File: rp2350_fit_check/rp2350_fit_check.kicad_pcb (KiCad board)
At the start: 6 copper layers, 118.8 x 73.4 mm, 667 parts, among them J1 Conn_01x05, J2 Conn_01x05, J3 Conn_01x05, J4 Conn_01x05, J5 Conn_01x04, SW1 SW_Push, SW2 SW_Push, U1 AP2112K-3.3, U2 RP2040, U3 W25Q16JVUXIQ_TR, Y1 12MHz, Y1 ABM8-272-T3

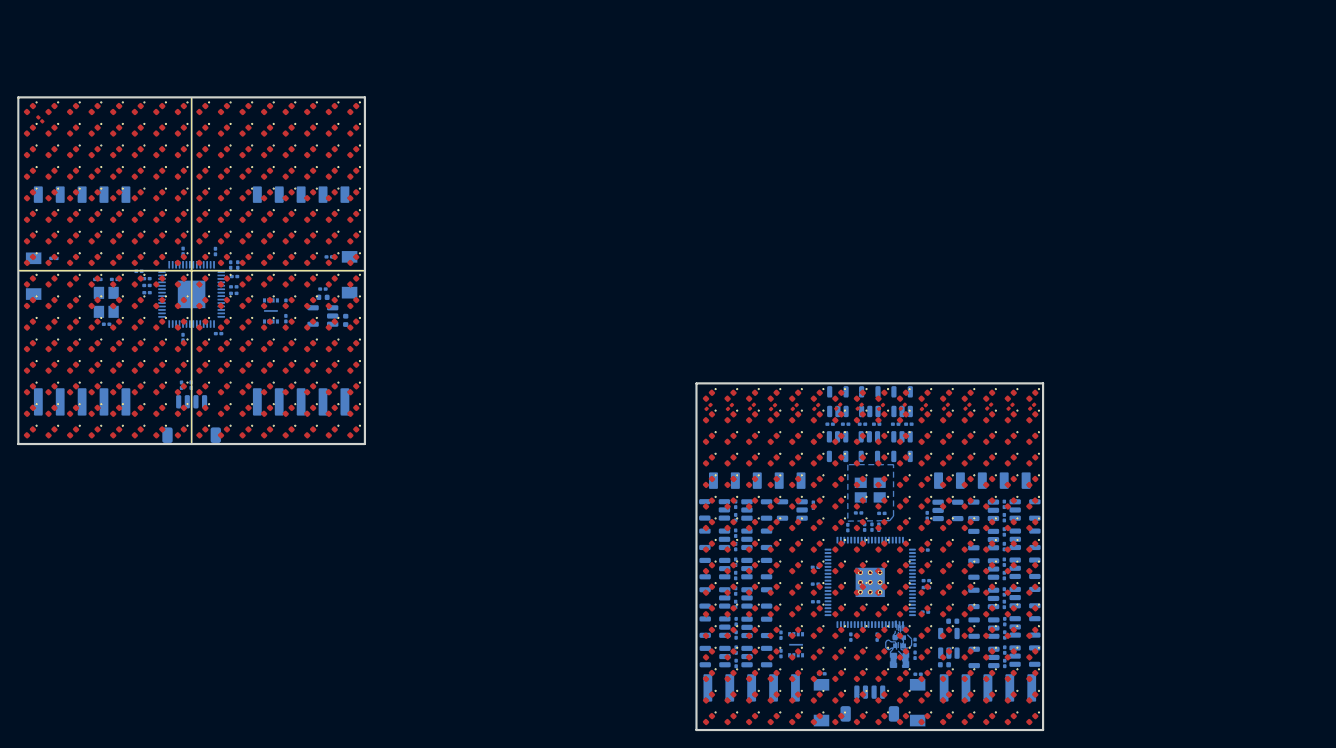
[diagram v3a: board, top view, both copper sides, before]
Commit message: Worked on new 18x18 led version of rp2350 design.
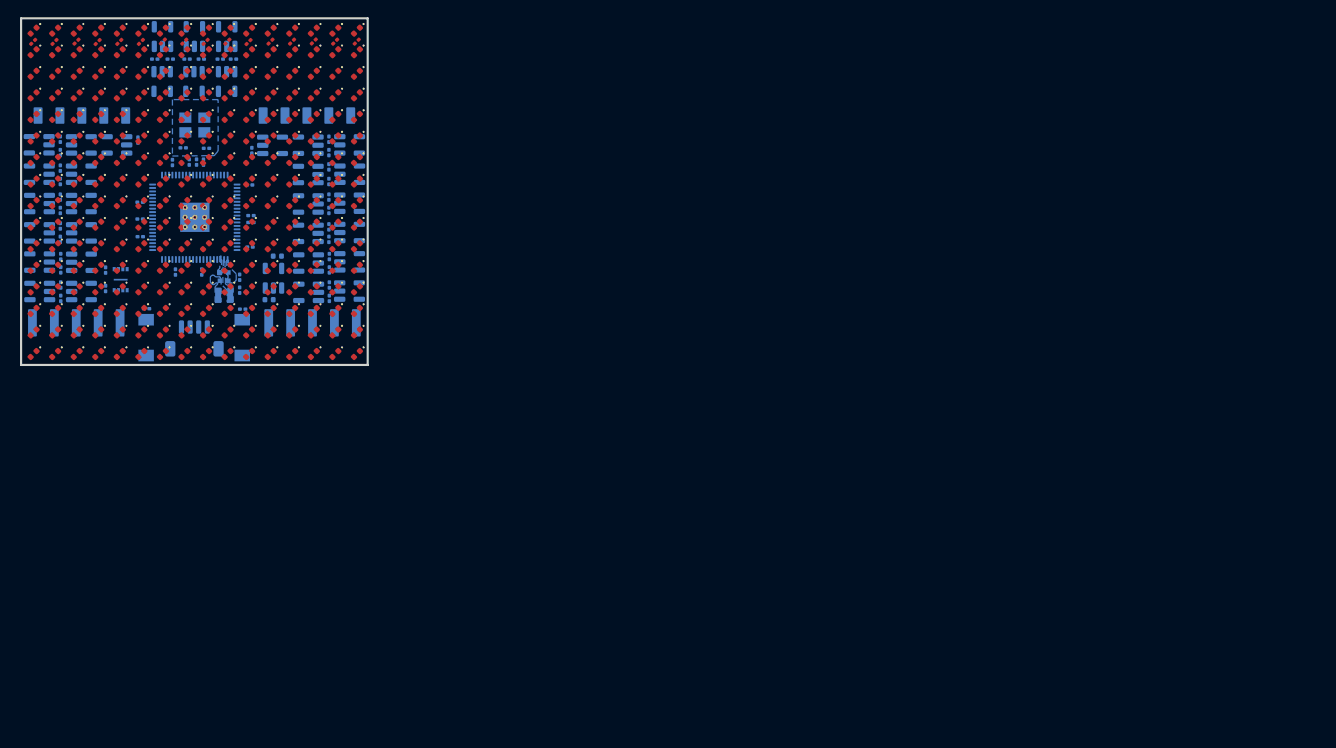
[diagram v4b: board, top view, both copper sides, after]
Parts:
- removed the C1 at (87.9, 75.8)
- removed C10, C9: 1uF, panel_custom:C_0201_0603Metric
- removed C11, C12, C13, C14, C15, C16, C17, C18, C19, C20, C3, C8: 0.1uF, panel_custom:C_0201_0603Metric
- removed the C2 at (85.2, 73.1)
- removed C4, C5: 20pF, panel_custom:C_0201_0603Metric
- removed the C6 at (75.3, 69.3)
- removed the C7 at (75.0, 70.7)
- removed the D1 at (51.2, 51.2)
- removed the D10 at (51.2, 73.8)
- removed the D100 at (66.2, 58.8)
- removed the D101 at (66.2, 61.2)
- removed the D102 at (66.2, 63.8)
- removed the D103 at (66.2, 66.2)
- removed the D104 at (66.2, 68.8)
- removed the D105 at (66.2, 71.2)
- removed the D106 at (66.2, 73.8)
- removed the D107 at (66.2, 76.2)
- removed the D108 at (66.2, 78.8)
- removed the D109 at (66.2, 81.2)
- removed the D11 at (51.2, 76.2)
- removed the D110 at (66.2, 83.8)
- removed the D111 at (66.2, 86.2)
- removed the D112 at (66.2, 88.8)
- removed the D113 at (68.8, 51.2)
- removed the D114 at (68.8, 53.8)
- removed the D115 at (68.8, 56.2)
- removed the D116 at (68.8, 58.8)
- removed the D117 at (68.8, 61.2)
- removed the D118 at (68.8, 63.8)
- removed the D119 at (68.8, 66.2)
- removed the D12 at (51.2, 78.8)
- removed the D120 at (68.8, 68.8)
- removed the D121 at (68.8, 71.2)
- removed the D122 at (68.8, 73.8)
- removed the D123 at (68.8, 76.2)
- removed the D124 at (68.8, 78.8)
- removed the D125 at (68.8, 81.2)
- removed the D126 at (68.8, 83.8)
- removed the D127 at (68.8, 86.2)
- removed the D128 at (68.8, 88.8)
- removed the D129 at (71.2, 51.2)
- removed the D13 at (51.2, 81.2)
- removed the D130 at (71.2, 53.8)
- removed the D131 at (71.2, 56.2)
- removed the D132 at (71.2, 58.8)
- removed the D133 at (71.2, 61.2)
- removed the D134 at (71.2, 63.8)
- removed the D135 at (71.2, 66.2)
- removed the D136 at (71.2, 68.8)
- removed the D137 at (71.2, 71.2)
- removed the D138 at (71.2, 73.8)
- removed the D139 at (71.2, 76.2)
- removed the D14 at (51.2, 83.8)
- removed the D140 at (71.2, 78.8)
- removed the D141 at (71.2, 81.2)
- removed the D142 at (71.2, 83.8)
- removed the D143 at (71.2, 86.2)
- removed the D144 at (71.2, 88.8)
- removed the D145 at (73.8, 51.2)
- removed the D146 at (73.8, 53.8)
- removed the D147 at (73.8, 56.2)
- removed the D148 at (73.8, 58.8)
- removed the D149 at (73.8, 61.2)
- removed the D15 at (51.2, 86.2)
- removed the D150 at (73.8, 63.8)
- removed the D151 at (73.8, 66.2)
- removed the D152 at (73.8, 68.8)
- removed the D153 at (73.8, 71.2)
- removed the D154 at (73.8, 73.8)
- removed the D155 at (73.8, 76.2)
- removed the D156 at (73.8, 78.8)
- removed the D157 at (73.8, 81.2)
- removed the D158 at (73.8, 83.8)
- removed the D159 at (73.8, 86.2)
- removed the D16 at (51.2, 88.8)
- removed the D160 at (73.8, 88.8)
- removed the D161 at (76.2, 51.2)
- removed the D162 at (76.2, 53.8)
- removed the D163 at (76.2, 56.2)
- removed the D164 at (76.2, 58.8)
- removed the D165 at (76.2, 61.2)
- removed the D166 at (76.2, 63.8)
- removed the D167 at (76.2, 66.2)
- removed the D168 at (76.2, 68.8)
- removed the D169 at (76.2, 71.2)
- removed the D17 at (53.8, 51.2)
- removed the D170 at (76.2, 73.8)
- removed the D171 at (76.2, 76.2)
- removed the D172 at (76.2, 78.8)
- removed the D173 at (76.2, 81.2)
- removed the D174 at (76.2, 83.8)
- removed the D175 at (76.2, 86.2)
- removed the D176 at (76.2, 88.8)
- removed the D177 at (78.8, 51.2)
- removed the D178 at (78.8, 53.8)
- removed the D179 at (78.8, 56.2)
- removed the D18 at (53.8, 53.8)
- removed the D180 at (78.8, 58.8)
- removed the D181 at (78.8, 61.2)
- removed the D182 at (78.8, 63.8)
- removed the D183 at (78.8, 66.2)
- removed the D184 at (78.8, 68.8)
- removed the D185 at (78.8, 71.2)
- removed the D186 at (78.8, 73.8)
- removed the D187 at (78.8, 76.2)
- removed the D188 at (78.8, 78.8)
- removed the D189 at (78.8, 81.2)
- removed the D19 at (53.8, 56.2)
- removed the D190 at (78.8, 83.8)
- removed the D191 at (78.8, 86.2)
- removed the D192 at (78.8, 88.8)
- removed the D193 at (81.2, 51.2)
- removed the D194 at (81.2, 53.8)
- removed the D195 at (81.2, 56.2)
- removed the D196 at (81.2, 58.8)
- removed the D197 at (81.2, 61.2)
- removed the D198 at (81.2, 63.8)
- removed the D199 at (81.2, 66.2)
- removed the D2 at (51.2, 53.8)
- removed the D20 at (53.8, 58.8)
- removed the D200 at (81.2, 68.8)
- removed the D201 at (81.2, 71.2)
- removed the D202 at (81.2, 73.8)
- removed the D203 at (81.2, 76.2)
- removed the D204 at (81.2, 78.8)
- removed the D205 at (81.2, 81.2)
- removed the D206 at (81.2, 83.8)
- removed the D207 at (81.2, 86.2)
- removed the D208 at (81.2, 88.8)
- removed the D209 at (83.8, 51.2)
- removed the D21 at (53.8, 61.2)
- removed the D210 at (83.8, 53.8)
- removed the D211 at (83.8, 56.2)
- removed the D212 at (83.8, 58.8)
- removed the D213 at (83.8, 61.2)
- removed the D214 at (83.8, 63.8)
- removed the D215 at (83.8, 66.2)
- removed the D216 at (83.8, 68.8)
- removed the D217 at (83.8, 71.2)
- removed the D218 at (83.8, 73.8)
- removed the D219 at (83.8, 76.2)
- removed the D22 at (53.8, 63.8)
- removed the D220 at (83.8, 78.8)
- removed the D221 at (83.8, 81.2)
- removed the D222 at (83.8, 83.8)
- removed the D223 at (83.8, 86.2)
- removed the D224 at (83.8, 88.8)
- removed the D225 at (86.2, 51.2)
- removed the D226 at (86.2, 53.8)
- removed the D227 at (86.2, 56.2)
- removed the D228 at (86.2, 58.8)
- removed the D229 at (86.2, 61.2)
- removed the D23 at (53.8, 66.2)
- removed the D230 at (86.2, 63.8)
- removed the D231 at (86.2, 66.2)
- removed the D232 at (86.2, 68.8)
- removed the D233 at (86.2, 71.2)
- removed the D234 at (86.2, 73.8)
- removed the D235 at (86.2, 76.2)
- removed the D236 at (86.2, 78.8)
- removed the D237 at (86.2, 81.2)
- removed the D238 at (86.2, 83.8)
- removed the D239 at (86.2, 86.2)
- removed the D24 at (53.8, 68.8)
- removed the D240 at (86.2, 88.8)
- removed the D241 at (88.8, 51.2)
- removed the D242 at (88.8, 53.8)
- removed the D243 at (88.8, 56.2)
- removed the D244 at (88.8, 58.8)
- removed the D245 at (88.8, 61.2)
- removed the D246 at (88.8, 63.8)
- removed the D247 at (88.8, 66.2)
- removed the D248 at (88.8, 68.8)
- removed the D249 at (88.8, 71.2)
- removed the D25 at (53.8, 71.2)
- removed the D250 at (88.8, 73.8)
- removed the D251 at (88.8, 76.2)
- removed the D252 at (88.8, 78.8)
- removed the D253 at (88.8, 81.2)
- removed the D254 at (88.8, 83.8)
- removed the D255 at (88.8, 86.2)
- removed the D256 at (88.8, 88.8)
- removed the D26 at (53.8, 73.8)
- removed the D27 at (53.8, 76.2)
- removed the D28 at (53.8, 78.8)
- removed the D29 at (53.8, 81.2)
- removed the D3 at (51.2, 56.2)
- removed the D30 at (53.8, 83.8)
- removed the D31 at (53.8, 86.2)
- removed the D32 at (53.8, 88.8)
- removed the D33 at (56.2, 51.2)
- removed the D34 at (56.2, 53.8)
- removed the D35 at (56.2, 56.2)
- removed the D36 at (56.2, 58.8)
- removed the D37 at (56.2, 61.2)
- removed the D38 at (56.2, 63.8)
- removed the D39 at (56.2, 66.2)
- removed the D4 at (51.2, 58.8)
- removed the D40 at (56.2, 68.8)
- removed the D41 at (56.2, 71.2)
- removed the D42 at (56.2, 73.8)
- removed the D43 at (56.2, 76.2)
- removed the D44 at (56.2, 78.8)
- removed the D45 at (56.2, 81.2)
- removed the D46 at (56.2, 83.8)
- removed the D47 at (56.2, 86.2)
- removed the D48 at (56.2, 88.8)
- removed the D49 at (58.8, 51.2)
- removed the D5 at (51.2, 61.2)
- removed the D50 at (58.8, 53.8)
- removed the D51 at (58.8, 56.2)
- removed the D52 at (58.8, 58.8)
- removed the D53 at (58.8, 61.2)
- removed the D54 at (58.8, 63.8)
- removed the D55 at (58.8, 66.2)
- removed the D56 at (58.8, 68.8)
- removed the D57 at (58.8, 71.2)
- removed the D58 at (58.8, 73.8)
- removed the D59 at (58.8, 76.2)
- removed the D6 at (51.2, 63.8)
- removed the D60 at (58.8, 78.8)
- removed the D61 at (58.8, 81.2)
- removed the D62 at (58.8, 83.8)
- removed the D63 at (58.8, 86.2)
- removed the D64 at (58.8, 88.8)
- removed the D65 at (61.2, 51.2)
- removed the D66 at (61.2, 53.8)
- removed the D67 at (61.2, 56.2)
- removed the D68 at (61.2, 58.8)
- removed the D69 at (61.2, 61.2)
- removed the D7 at (51.2, 66.2)
- removed the D70 at (61.2, 63.8)
- removed the D71 at (61.2, 66.2)
- removed the D72 at (61.2, 68.8)
- removed the D73 at (61.2, 71.2)
- removed the D74 at (61.2, 73.8)
- removed the D75 at (61.2, 76.2)
- removed the D76 at (61.2, 78.8)
- removed the D77 at (61.2, 81.2)
- removed the D78 at (61.2, 83.8)
- removed the D79 at (61.2, 86.2)
- removed the D8 at (51.2, 68.8)
- removed the D80 at (61.2, 88.8)
- removed the D81 at (63.8, 51.2)
- removed the D82 at (63.8, 53.8)
- removed the D83 at (63.8, 56.2)
- removed the D84 at (63.8, 58.8)
- removed the D85 at (63.8, 61.2)
- removed the D86 at (63.8, 63.8)
- removed the D87 at (63.8, 66.2)
- removed the D88 at (63.8, 68.8)
- removed the D89 at (63.8, 71.2)
- removed the D9 at (51.2, 71.2)
- removed the D90 at (63.8, 73.8)
- removed the D91 at (63.8, 76.2)
- removed the D92 at (63.8, 78.8)
- removed the D93 at (63.8, 81.2)
- removed the D94 at (63.8, 83.8)
- removed the D95 at (63.8, 86.2)
- removed the D96 at (63.8, 88.8)
- removed the D97 at (66.2, 51.2)
- removed the D98 at (66.2, 53.8)
- removed the D99 at (66.2, 56.2)
- removed the J1 at (82.7, 85.2)
- removed the J2 at (57.3, 85.2)
- removed the J3 at (82.7, 53.9)
- removed the J4 at (57.3, 53.9)
- removed J5: Conn_01x04, panel_custom:JST_SH_SM04B-SRSS-TB_1x04-1MP_P1.00mm_Horizontal
- removed R1, R2: 27.4, panel_custom:R_0201_0603Metric
- removed R3, R4: 1k, panel_custom:R_0201_0603Metric
- removed R5: 10k, panel_custom:R_0201_0603Metric
- removed the REF** at (52.5, 52.5)
- removed the SW1 at (51.7, 70.6)
- removed the SW2 at (88.3, 70.5)
- removed the U1 at (85.2, 75.3)
- removed U2: RP2040, Package_DFN_QFN:QFN-56-1EP_7x7mm_P0.4mm_EP3.2x3.2mm
- removed U3: W25Q16JVUXIQ_TR, panel_custom:flashmem_PSON50P300X200X60-9N
- removed the Y1 at (60.1, 73.7)
- moved ? 89.0 mm to (73.3, 70.2)
- moved C2 89.0 mm to (79.9, 68.3)
- moved REF** 89.0 mm to (54.1, 43.5)
- moved REF** 89.0 mm to (69.5, 45.5)
- moved REF** 89.0 mm to (88.3, 55.4)
- moved REF** 89.0 mm to (76.6, 43.5)
- moved REF** 89.0 mm to (88.3, 65.6)
- moved REF** 89.0 mm to (75.6, 70.8)
- moved REF** 89.0 mm to (88.3, 62.2)
- moved REF** 89.0 mm to (57.2, 65.6)
- moved REF** 89.0 mm to (57.2, 69.0)
- moved REF** 89.0 mm to (70.3, 42.8)
- moved REF** 89.0 mm to (65.7, 45.5)
- moved REF** 89.0 mm to (76.7, 60.1)
- moved REF** 89.0 mm to (86.0, 73.2)
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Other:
- board size 118.8 x 73.4 mm -> 40.2 x 40.2 mm
- board text removed: "BOOT"
- board text removed: "Panel G6 V1.0R1"
- board text removed: "RST"
